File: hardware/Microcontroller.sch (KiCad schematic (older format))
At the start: 22 parts, among them J2 Conn_01x06_Male, J3 USB_B, SW1 SW_Push, U1 PIC18F4550-IP, U12 H11AA1, U13 H11AA1

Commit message: Update schematic for Issue 2.
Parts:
- C3: value NP -> 0.01uF
- R1: value 10K -> 4.7K
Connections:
- net labels added: USB_D+, USB_D-
- net labels removed: USB_DM, USB_DP
- no-connect marks 9 -> 11
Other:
- note added: "2"
- note added: "2020-05-24"
- note added: "Layout note:\nReset circuit should be close to the pin on the MCU."
- note removed: "1"
- note removed: "2020-05-17"
- moved on the sheet: J2
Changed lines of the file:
@@
 AR Path="/5EC2B537" Ref="C?"  Part="1"
 AR Path="/5EBEBADD/5EC2B537" Ref="C3"  Part="1"
-F 0 "C3" H 6715 5896 50  0000 L CNN
-F 1 "NP" H 6715 5805 50  0000 L CNN
+F 0 "C3" H 6300 5950 50  0000 L CNN
+F 1 "0.01uF" H 6150 5850 50  0000 L CNN
 F 2 "Capacitor_THT:C_Disc_D3.0mm_W1.6mm_P2.50mm" H 6638 5700 50  0001 C CNN
 F 3 "~" H 6600 5850 50  0001 C CNN
@@
 AR Path="/5EBEBADD/5EC2B545" Ref="R1"  Part="1"
 F 0 "R1" V 6945 5650 50  0000 C CNN
-F 1 "10K" V 7036 5650 50  0000 C CNN
+F 1 "4.7K" V 7036 5650 50  0000 C CNN
 F 2 "Resistor_THT:R_Axial_DIN0207_L6.3mm_D2.5mm_P7.62mm_Horizontal" V 7190 5640 50  0001 C CNN
 F 3 "~" H 7150 5650 50  0001 C CNN
@@
 L Connector:Conn_01x06_Male J?
 U 1 1 5EC2B556
-P 2450 4550
+P 2550 4950
 AR Path="/5EC2B556" Ref="J?"  Part="1"
 AR Path="/5EBEBADD/5EC2B556" Ref="J2"  Part="1"
-F 0 "J2" H 2558 4931 50  0000 C CNN
-F 1 "Conn_01x06_Male" H 2558 4840 50  0000 C CNN
-F 2 "Connector_PinHeader_2.54mm:PinHeader_1x06_P2.54mm_Vertical" H 2450 4550 50  0001 C CNN
-F 3 "~" H 2450 4550 50  0001 C CNN
-	1    2450 4550
-	1    0    0    -1
+F 0 "J2" H 2658 5331 50  0000 C CNN
+F 1 "Conn_01x06_Male" H 2658 5240 50  0000 C CNN
+F 2 "Connector_PinHeader_2.54mm:PinHeader_1x06_P2.54mm_Vertical" H 2550 4950 50  0001 C CNN
+F 3 "~" H 2550 4950 50  0001 C CNN
+	1    2550 4950
+	1    0    0    1
 $EndComp
 $Comp
 L power:GND #PWR?
 U 1 1 5EC2B55C
-P 2850 4550
+P 3400 5150
 AR Path="/5EC2B55C" Ref="#PWR?"  Part="1"
 AR Path="/5EBEBADD/5EC2B55C" Ref="#PWR06"  Part="1"
-F 0 "#PWR06" H 2850 4300 50  0001 C CNN
-F 1 "GND" H 2855 4377 50  0000 C CNN
-F 2 "" H 2850 4550 50  0001 C CNN
-F 3 "" H 2850 4550 50  0001 C CNN
-	1    2850 4550
-	1    0    0    -1
-$EndComp
-Wire Wire Line
-	2650 4550 2850 4550
+F 0 "#PWR06" H 3400 4900 50  0001 C CNN
+F 1 "GND" H 3405 4977 50  0000 C CNN
+F 2 "" H 3400 5150 50  0001 C CNN
+F 3 "" H 3400 5150 50  0001 C CNN
+	1    3400 5150
+	1    0    0    -1
+$EndComp
 $Comp
 L power:+5V #PWR?
@@
 L power:+5V #PWR?
 U 1 1 5EC2B569
-P 2850 4450
+P 2900 4500
 AR Path="/5EC2B569" Ref="#PWR?"  Part="1"
 AR Path="/5EBEBADD/5EC2B569" Ref="#PWR05"  Part="1"
-F 0 "#PWR05" H 2850 4300 50  0001 C CNN
-F 1 "+5V" H 2865 4623 50  0000 C CNN
-F 2 "" H 2850 4450 50  0001 C CNN
-F 3 "" H 2850 4450 50  0001 C CNN
-	1    2850 4450
-	1    0    0    -1
-$EndComp
-Wire Wire Line
-	2850 4450 2650 4450
-Wire Wire Line
-	2650 4850 4250 4850
-Wire Wire Line
-	2650 4750 4250 4750
-Wire Wire Line
-	2650 4350 3200 4350
-Wire Wire Line
-	3200 4350 3200 6500
+F 0 "#PWR05" H 2900 4350 50  0001 C CNN
+F 1 "+5V" H 2915 4673 50  0000 C CNN
+F 2 "" H 2900 4500 50  0001 C CNN
+F 3 "" H 2900 4500 50  0001 C CNN
+	1    2900 4500
+	1    0    0    -1
+$EndComp
 Wire Wire Line
 	3200 6500 6450 6500
@@
 	7000 5650 6900 5650
 Connection ~ 6900 5650
-Wire Wire Line
-	4000 4550 4250 4550
-Wire Wire Line
-	4000 4450 4250 4450
-NoConn ~ 2650 4650
 Text Label 6950 3650 0    50   ~ 0
 UART_TX
@@
 	7550 1250 7550 3550
 Text Label 6950 3450 0    50   ~ 0
-USB_DM
+USB_D-
 Text Label 6950 3550 0    50   ~ 0
-USB_DP
+USB_D+
 Text Label 3600 4750 0    50   ~ 0
 ICSP_PGC
@@
 	2950 2400 2600 2400
 Wire Wire Line
-	2600 1800 3350 1800
-Wire Wire Line
-	2600 1900 3250 1900
-Wire Wire Line
-	2600 2000 3150 2000
-Wire Wire Line
-	2600 2100 3050 2100
+	2600 1800 3100 1800
+Wire Wire Line
+	2600 1900 3100 1900
+Wire Wire Line
+	2600 2000 3100 2000
+Wire Wire Line
+	2600 2100 3100 2100
 Wire Wire Line
 	2600 2900 2850 2900
@@
 Text Label 6900 5050 0    50   ~ 0
 DTMF0_Q3
-Text Label 2650 2100 0    50   ~ 0
+Text Label 3100 2100 0    50   ~ 0
 DTMF0_Q3
-Text Label 2650 2000 0    50   ~ 0
+Text Label 3100 2000 0    50   ~ 0
 DTMF0_Q2
-Text Label 2650 1900 0    50   ~ 0
+Text Label 3100 1900 0    50   ~ 0
 DTMF0_Q1
-Text Label 2650 1800 0    50   ~ 0
+Text Label 3100 1800 0    50   ~ 0
 DTMF0_Q0
 Wire Wire Line
@@
 Wire Wire Line
 	2600 2700 3100 2700
-Text Label 2650 2700 0    50   ~ 0
+Text Label 3100 2700 0    50   ~ 0
 DTMF1_Q1
 Wire Wire Line
 	3100 2600 2600 2600
-Text Label 2650 2600 0    50   ~ 0
+Text Label 3100 2600 0    50   ~ 0
 DTMF1_Q0
 Wire Wire Line
@@
 Wire Wire Line
 	3100 2800 2600 2800
-Text Label 2650 2800 0    50   ~ 0
+Text Label 3100 2800 0    50   ~ 0
 DTMF1_Q2
 Wire Wire Line
@@
 OKI AC125A DTMF Converter - Microcontroller and Peripherals
 Text Notes 8150 7650 0    50   ~ 0
-2020-05-17
+2020-05-24
 Text Notes 10550 7650 0    50   ~ 0
-1
+2
 Text Notes 8300 1300 0    50   ~ 0
 OR0 Active
@@
 	9250 1650 9400 1650
 NoConn ~ 6450 3350
+Wire Wire Line
+	3200 6500 3200 5150
+Wire Wire Line
+	3200 5150 2750 5150
+Wire Wire Line
+	2750 5050 2900 5050
+Wire Wire Line
+	2900 5050 2900 4500
+Wire Wire Line
+	2750 4950 3400 4950
+Wire Wire Line
+	3400 4950 3400 5150
+Wire Wire Line
+	2750 4850 4250 4850
+Wire Wire Line
+	2750 4750 4250 4750
+NoConn ~ 2750 4650
+Text Notes 7000 6150 0    50   Italic 0
+Layout note:\nReset circuit should be close to the pin on the MCU.
+NoConn ~ 4250 4550
+NoConn ~ 4250 4450
 $EndSCHEMATC

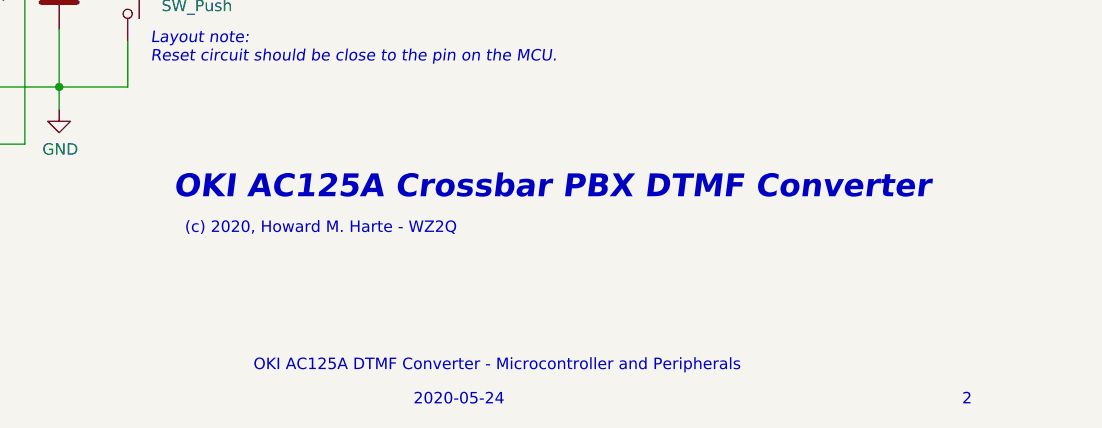
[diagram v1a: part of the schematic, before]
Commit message: Final schematic and PCB layout for Issue 2.
Corrected errors in Issue 1 and fabbed out the PCB.
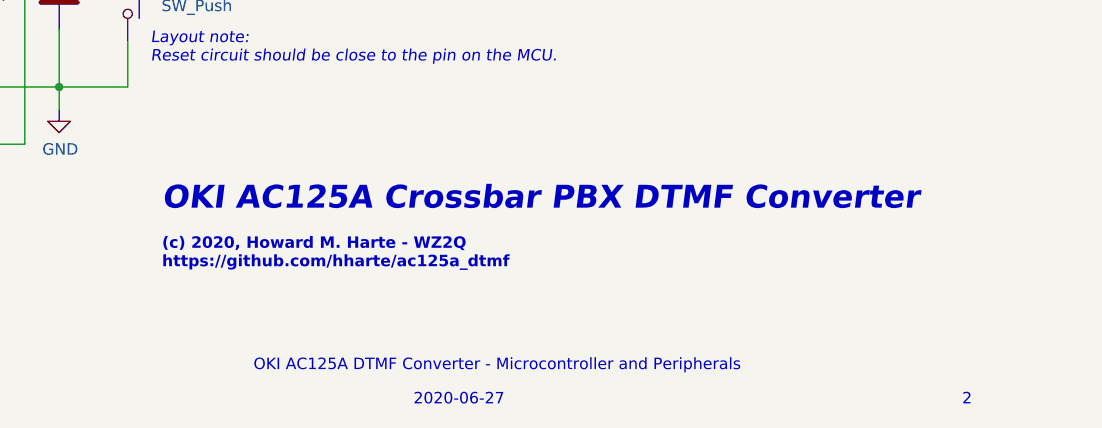
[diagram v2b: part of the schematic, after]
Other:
- note added: "(c) 2020, Howard M. Harte - WZ2Q\nhttps://github.com/hharte/ac125a_dtmf"
- note added: "2020-06-27"
- note removed: "(c) 2020, Howard M. Harte - WZ2Q"
- note removed: "2020-05-24"
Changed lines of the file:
@@
 $EndDescr
-$Comp
-L power:+5V #PWR?
-U 1 1 5EC2B51D
-P 3950 800
-AR Path="/5EC2B51D" Ref="#PWR?"  Part="1"
-AR Path="/5EBEBADD/5EC2B51D" Ref="#PWR01"  Part="1"
-F 0 "#PWR01" H 3950 650 50  0001 C CNN
-F 1 "+5V" H 3965 973 50  0000 C CNN
-F 2 "" H 3950 800 50  0001 C CNN
-F 3 "" H 3950 800 50  0001 C CNN
-	1    3950 800
-	1    0    0    -1
-$EndComp
 $Comp
 L MCU_Microchip_PIC18:PIC18F4550-IP U?
@@
 	6450 6500 6450 5350
 Connection ~ 6450 5350
-$Comp
-L Device:C C?
-U 1 1 5EC2B577
-P 3950 1000
-AR Path="/5EC2B577" Ref="C?"  Part="1"
-AR Path="/5EBEBADD/5EC2B577" Ref="C1"  Part="1"
-F 0 "C1" H 4065 1046 50  0000 L CNN
-F 1 "0.1uF" H 4065 955 50  0000 L CNN
-F 2 "Capacitor_THT:C_Disc_D3.0mm_W2.0mm_P2.50mm" H 3988 850 50  0001 C CNN
-F 3 "https://www.digikey.com/product-detail/en/vishay-bc-components/K104Z15Y5VE5TL2/BC1148CT-ND/286770" H 3950 1000 50  0001 C CNN
-	1    3950 1000
-	1    0    0    -1
-$EndComp
-$Comp
-L power:GND #PWR?
-U 1 1 5EC2B57D
-P 3950 1200
-AR Path="/5EC2B57D" Ref="#PWR?"  Part="1"
-AR Path="/5BA49F1B/5EC2B57D" Ref="#PWR?"  Part="1"
-AR Path="/5EBEBADD/5EC2B57D" Ref="#PWR02"  Part="1"
-F 0 "#PWR02" H 3950 950 50  0001 C CNN
-F 1 "GND" H 3955 1027 50  0000 C CNN
-F 2 "" H 3950 1200 50  0001 C CNN
-F 3 "" H 3950 1200 50  0001 C CNN
-	1    3950 1200
-	1    0    0    -1
-$EndComp
-Wire Wire Line
-	3950 850  3950 800
-Wire Wire Line
-	3950 1150 3950 1200
 $Comp
 L Device:C C?
@@
 Wire Wire Line
 	7850 1050 8100 1050
-$Comp
-L ac125a_dtmf:DMC-16105-LY LCD1
-U 1 1 5EE28C31
-P 5550 1550
-F 0 "LCD1" H 5994 1596 50  0000 L CNN
-F 1 "DMC-16105-LY" H 5994 1505 50  0000 L CNN
-F 2 "Connector_PinHeader_2.54mm:PinHeader_1x15_P2.54mm_Vertical" H 5550 750 50  0001 C CNN
-F 3 "https://media.digikey.com/pdf/data%20sheets/optrex%20pdfs/dmc-16105ny-ly-ann.pdf" H 5650 1450 50  0001 C CNN
-	1    5550 1550
-	1    0    0    -1
-$EndComp
 Wire Wire Line
 	7900 4450 8650 4450
@@
 Wire Wire Line
 	7900 4150 8650 4150
+Text Label 7900 4150 0    50   ~ 0
+SSR_SER_DATA
+Text Label 3300 3150 0    50   ~ 0
+SSR_SER_DATA
+Text Label 7900 4450 0    50   ~ 0
+SSR_OE_
+Wire Wire Line
+	8650 4250 7900 4250
+Text Label 7900 4250 0    50   ~ 0
+SSR_SRCLK
+Text Label 7900 4350 0    50   ~ 0
+SSR_RCLK
+Text Label 3850 3450 0    50   ~ 0
+SSR_SRCLK
+Text Label 3850 3350 0    50   ~ 0
+SSR_RCLK
+Wire Wire Line
+	6900 4350 6450 4350
+Wire Wire Line
+	6900 4250 6450 4250
+Wire Wire Line
+	6900 4150 6450 4150
+Text Label 6900 4350 0    50   ~ 0
+LCD_RS
+Text Label 6900 4450 0    50   ~ 0
+LCD_RW
+Wire Wire Line
+	6900 4450 6450 4450
+Wire Wire Line
+	6900 4550 6450 4550
+Text Label 6900 4550 0    50   ~ 0
+LCD_E
+Text Label 6900 4150 0    50   ~ 0
+LCD_DB7
+Text Label 6900 4250 0    50   ~ 0
+LCD_DB6
+Wire Wire Line
+	3650 4650 4250 4650
+Text Label 3650 4650 0    50   ~ 0
+LCD_DB4
+Wire Wire Line
+	4250 3750 3700 3750
+Text Label 3700 3750 0    50   ~ 0
+LCD_DB5
+Text Notes 7450 7500 0    50   ~ 0
+OKI AC125A DTMF Converter - Microcontroller and Peripherals
+Text Notes 8150 7650 0    50   ~ 0
+2020-06-27
+Text Notes 10550 7650 0    50   ~ 0
+2
+Text Notes 8300 1300 0    50   ~ 0
+OR0 Active
+Text Notes 8350 3050 0    50   ~ 0
+OR1 Active
+Text Notes 7050 6800 0    100  Italic 20
+OKI AC125A Crossbar PBX DTMF Converter
+Wire Wire Line
+	9250 1750 9250 1650
+Wire Wire Line
+	9250 1650 9400 1650
+NoConn ~ 6450 3350
+Wire Wire Line
+	3200 6500 3200 5150
+Wire Wire Line
+	3200 5150 2750 5150
+Wire Wire Line
+	2750 5050 2900 5050
+Wire Wire Line
+	2900 5050 2900 4500
+Wire Wire Line
+	2750 4950 3400 4950
+Wire Wire Line
+	3400 4950 3400 5150
+Wire Wire Line
+	2750 4850 4250 4850
+Wire Wire Line
+	2750 4750 4250 4750
+NoConn ~ 2750 4650
+Text Notes 7000 6150 0    50   Italic 0
+Layout note:\nReset circuit should be close to the pin on the MCU.
+NoConn ~ 4250 4550
+NoConn ~ 4250 4450
+Wire Wire Line
+	5550 2300 5550 2250
 $Comp
 L power:GND #PWR0118
@@
 	1    0    0    -1
 $EndComp
-Wire Wire Line
-	5550 2300 5550 2250
+Text Label 4350 2050 0    50   ~ 0
+LCD_DB7
+Text Label 4350 1950 0    50   ~ 0
+LCD_DB6
+Text Label 4350 1850 0    50   ~ 0
+LCD_DB5
+Text Label 4350 1750 0    50   ~ 0
+LCD_DB4
+Text Label 4350 1250 0    50   ~ 0
+LCD_E
+Text Label 4350 1150 0    50   ~ 0
+LCD_RW
+Text Label 4350 1050 0    50   ~ 0
+LCD_RS
+Wire Wire Line
+	4350 2050 5150 2050
+Wire Wire Line
+	4350 1950 5150 1950
+Wire Wire Line
+	4350 1850 5150 1850
+Wire Wire Line
+	4350 1750 5150 1750
+Wire Wire Line
+	4350 1250 5150 1250
+Wire Wire Line
+	4350 1150 5150 1150
+Wire Wire Line
+	4350 1050 5150 1050
+NoConn ~ 5150 1650
+NoConn ~ 5150 1550
+NoConn ~ 5150 1450
+NoConn ~ 5150 1350
+Wire Wire Line
+	5550 850  5550 800
 $Comp
 L power:+5V #PWR?
@@
 	1    0    0    -1
 $EndComp
-Wire Wire Line
-	5550 850  5550 800
-NoConn ~ 5150 1350
-NoConn ~ 5150 1450
-NoConn ~ 5150 1550
-NoConn ~ 5150 1650
-Text Label 7900 4150 0    50   ~ 0
-SSR_SER_DATA
-Text Label 3300 3150 0    50   ~ 0
-SSR_SER_DATA
-Text Label 7900 4450 0    50   ~ 0
-SSR_OE_
-Wire Wire Line
-	8650 4250 7900 4250
-Text Label 7900 4250 0    50   ~ 0
-SSR_SRCLK
-Text Label 7900 4350 0    50   ~ 0
-SSR_RCLK
-Text Label 3850 3450 0    50   ~ 0
-SSR_SRCLK
-Text Label 3850 3350 0    50   ~ 0
-SSR_RCLK
-Wire Wire Line
-	4350 1050 5150 1050
-Wire Wire Line
-	4350 1150 5150 1150
-Wire Wire Line
-	4350 1250 5150 1250
-Wire Wire Line
-	4350 1750 5150 1750
-Wire Wire Line
-	4350 1850 5150 1850
-Wire Wire Line
-	4350 1950 5150 1950
-Wire Wire Line
-	4350 2050 5150 2050
-Text Label 4350 1050 0    50   ~ 0
-LCD_RS
-Text Label 4350 1150 0    50   ~ 0
-LCD_RW
-Text Label 4350 1250 0    50   ~ 0
-LCD_E
-Text Label 4350 1750 0    50   ~ 0
-LCD_DB4
-Text Label 4350 1850 0    50   ~ 0
-LCD_DB5
-Text Label 4350 1950 0    50   ~ 0
-LCD_DB6
-Text Label 4350 2050 0    50   ~ 0
-LCD_DB7
-Wire Wire Line
-	6900 4350 6450 4350
-Wire Wire Line
-	6900 4250 6450 4250
-Wire Wire Line
-	6900 4150 6450 4150
-Text Label 6900 4350 0    50   ~ 0
-LCD_RS
-Text Label 6900 4450 0    50   ~ 0
-LCD_RW
-Wire Wire Line
-	6900 4450 6450 4450
-Wire Wire Line
-	6900 4550 6450 4550
-Text Label 6900 4550 0    50   ~ 0
-LCD_E
-Text Label 6900 4150 0    50   ~ 0
-LCD_DB7
-Text Label 6900 4250 0    50   ~ 0
-LCD_DB6
-Wire Wire Line
-	3650 4650 4250 4650
-Text Label 3650 4650 0    50   ~ 0
-LCD_DB4
-Wire Wire Line
-	4250 3750 3700 3750
-Text Label 3700 3750 0    50   ~ 0
-LCD_DB5
-Text Notes 7450 7500 0    50   ~ 0
-OKI AC125A DTMF Converter - Microcontroller and Peripherals
-Text Notes 8150 7650 0    50   ~ 0
-2020-05-24
-Text Notes 10550 7650 0    50   ~ 0
-2
-Text Notes 8300 1300 0    50   ~ 0
-OR0 Active
-Text Notes 8350 3050 0    50   ~ 0
-OR1 Active
-Text Notes 7100 6750 0    100  Italic 20
-OKI AC125A Crossbar PBX DTMF Converter
-Text Notes 7150 6900 0    50   ~ 0
-(c) 2020, Howard M. Harte - WZ2Q
-Wire Wire Line
-	9250 1750 9250 1650
-Wire Wire Line
-	9250 1650 9400 1650
-NoConn ~ 6450 3350
-Wire Wire Line
-	3200 6500 3200 5150
-Wire Wire Line
-	3200 5150 2750 5150
-Wire Wire Line
-	2750 5050 2900 5050
-Wire Wire Line
-	2900 5050 2900 4500
-Wire Wire Line
-	2750 4950 3400 4950
-Wire Wire Line
-	3400 4950 3400 5150
-Wire Wire Line
-	2750 4850 4250 4850
-Wire Wire Line
-	2750 4750 4250 4750
-NoConn ~ 2750 4650
-Text Notes 7000 6150 0    50   Italic 0
-Layout note:\nReset circuit should be close to the pin on the MCU.
-NoConn ~ 4250 4550
-NoConn ~ 4250 4450
+$Comp
+L ac125a_dtmf:DMC-16105-LY LCD1
+U 1 1 5EE28C31
+P 5550 1550
+F 0 "LCD1" H 5994 1596 50  0000 L CNN
+F 1 "DMC-16105-LY" H 5994 1505 50  0000 L CNN
+F 2 "Connector_PinHeader_2.54mm:PinHeader_1x15_P2.54mm_Vertical" H 5550 750 50  0001 C CNN
+F 3 "https://media.digikey.com/pdf/data%20sheets/optrex%20pdfs/dmc-16105ny-ly-ann.pdf" H 5650 1450 50  0001 C CNN
+	1    5550 1550
+	1    0    0    -1
+$EndComp
+Wire Wire Line
+	3950 1150 3950 1200
+Wire Wire Line
+	3950 850  3950 800
+$Comp
+L power:GND #PWR?
+U 1 1 5EC2B57D
+P 3950 1200
+AR Path="/5EC2B57D" Ref="#PWR?"  Part="1"
+AR Path="/5BA49F1B/5EC2B57D" Ref="#PWR?"  Part="1"
+AR Path="/5EBEBADD/5EC2B57D" Ref="#PWR02"  Part="1"
+F 0 "#PWR02" H 3950 950 50  0001 C CNN
+F 1 "GND" H 3955 1027 50  0000 C CNN
+F 2 "" H 3950 1200 50  0001 C CNN
+F 3 "" H 3950 1200 50  0001 C CNN
+	1    3950 1200
+	1    0    0    -1
+$EndComp
+$Comp
+L Device:C C?
+U 1 1 5EC2B577
+P 3950 1000
+AR Path="/5EC2B577" Ref="C?"  Part="1"
+AR Path="/5EBEBADD/5EC2B577" Ref="C1"  Part="1"
+F 0 "C1" H 4065 1046 50  0000 L CNN
+F 1 "0.1uF" H 4065 955 50  0000 L CNN
+F 2 "Capacitor_THT:C_Disc_D3.0mm_W2.0mm_P2.50mm" H 3988 850 50  0001 C CNN
+F 3 "https://www.digikey.com/product-detail/en/vishay-bc-components/K104Z15Y5VE5TL2/BC1148CT-ND/286770" H 3950 1000 50  0001 C CNN
+	1    3950 1000
+	1    0    0    -1
+$EndComp
+$Comp
+L power:+5V #PWR?
+U 1 1 5EC2B51D
+P 3950 800
+AR Path="/5EC2B51D" Ref="#PWR?"  Part="1"
+AR Path="/5EBEBADD/5EC2B51D" Ref="#PWR01"  Part="1"
+F 0 "#PWR01" H 3950 650 50  0001 C CNN
+F 1 "+5V" H 3965 973 50  0000 C CNN
+F 2 "" H 3950 800 50  0001 C CNN
+F 3 "" H 3950 800 50  0001 C CNN
+	1    3950 800
+	1    0    0    -1
+$EndComp
+Text Notes 7050 7050 0    50   ~ 10
+(c) 2020, Howard M. Harte - WZ2Q\nhttps://github.com/hharte/ac125a_dtmf
 $EndSCHEMATC
